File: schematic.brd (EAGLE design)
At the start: 50.5 x 50.8 mm, 32 parts, among them IC1 FT230XS, IC2 ATMEGA644A, IC4 L4931D, X1 MINI-USB-32005-301

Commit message: saving to git
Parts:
- added C11: .1uf, eagle-ltspice:C0504
- added C12, C13, C17: 1uF, eagle-ltspice:C0504
- added C14, C15: 2.2uF, eagle-ltspice:C0504
- added C16: .1uF, eagle-ltspice:C0504
- added R12, R13: 2K, eagle-ltspice:R0603
- added R14: 390K, eagle-ltspice:R0603
- added U$3: UG-2864HSWEG01, adafruit:1X30-0.7MM
- moved C10 29.2 mm to (64.8, 16.5)
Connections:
- new net N$10: C13.1, U$3.3
- new net N$11: C17.2, U$3.4
- new net N$12: C17.1, U$3.5
- new net N$5: C14.2, U$3.27
- new net N$7: C13.2, U$3.2
- new net N$9: R14.1, U$3.26
- new net OLED_SCL: R12.1, U$3.18
- new net OLED_SDA: R13.1, U$3.19, U$3.20
- new net OLED_VCC: C15.2, C16.2, U$3.28
- new net OLED_VDD: C11.2, C12.2, R12.2, R13.2, U$3.11, U$3.14, U$3.6, U$3.9
- new net OLED_VSS: U$3.10, U$3.12, U$3.13, U$3.16
- net GND: now also C11.1, C12.1, C14.1, C15.1, C16.1, R14.2, U$3.15, U$3.17, U$3.29, U$3.8

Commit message: saving
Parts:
- removed IC2: ATMEGA644A, atmel:TQFP44
- added C18: 1uF, eagle-ltspice:C0504
- added IC3: ATMEGA32U2-TQFP, adafruit:TQFP32-08
- added JP1: (no value), adafruit:1X06-BIG
- added R15, R16: 22, eagle-ltspice:R0603
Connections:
- removed net AVCC: IC2.27
- new net N$13: IC3.17, JP1.4
- new net N$14: C18.2, IC3.27
- new net N$15: IC3.30, R15.1
- new net N$16: IC3.29, R16.1
- new net N$3: IC3.15, JP1.2
- new net N$4: IC3.16, JP1.3
- new net RESET: IC3.24, JP1.5
- new net UGND: IC3.28, X1.4
- new net VUSB: C1.1, U$1.1, U$1.4, X1.1
- net B0: no longer IC2.11
- net B1: no longer IC2.12
- net B2: no longer IC2.13
- net GND: now also C18.1, IC3.3, JP1.6, U$3.1, U$3.30; no longer IC2.18, IC2.28, IC2.39, IC2.6, X1.4
- net OLED_VDD: no longer C11.2, C12.2, U$3.6, U$3.9
- net USB+: now also R16.2
- net USB-: now also R15.2
- net VCC: now also C11.2, C12.2, IC3.4, JP1.1, U$3.6, U$3.9; no longer IC2.17, IC2.38, IC2.5
- net VCHG: no longer C1.1, U$1.1, U$1.4, X1.1

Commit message: Saving to git
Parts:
- removed IC3: ATMEGA32U2-TQFP, adafruit:TQFP32-08
- removed R15, R16: 22, eagle-ltspice:R0603
- removed S1, S4, S5: (no value), switch-omron:B3F-10XX
- removed SV1: (no value), con-lsta:FE05-1
- removed U$2: RN4020, microchip_bluetooth_v101:RN4020SMD
- added JP2: (no value), pinhead:1X02
- added JP3: (no value), adafruit:1X03
- added LED1, LED2, LED3: (no value), adafruit:1206
- added R17, R18, R19: 2K, eagle-ltspice:R0603
- added SW1, SW2, SW3: (no value), adafruit:PUSHBUTTON_SMD_SJ
- added U$4: ATMEGA32U4-AU, adafruit:TQFP44
- U$1: value MCP73812T-420I/OT -> (none)
- moved C18 174.1 mm to (50.8, 67.3)
- moved JP1 174.1 mm to (64.1, 79.4)
- moved C14 101.1 mm to (54.0, 47.6)
- moved C15 101.1 mm to (54.0, 41.3)
- moved C16 101.1 mm to (54.0, 34.9)
- moved C17 101.1 mm to (54.0, 23.5)
- moved R14 101.1 mm to (54.0, 29.2)
- moved C12 81.8 mm to (59.7, 30.5)
- moved R13 81.8 mm to (59.7, 42.5)
- moved C11 81.8 mm to (59.7, 36.8)
- moved C13 81.8 mm to (59.7, 24.1)
- moved R12 81.8 mm to (59.7, 47.6)
- moved C6 15.3 mm to (40.0, 15.2)
- moved U$1 7.65 mm to (41.3, 38.1)
- moved C2 5.24 mm to (40.6, 12.7)
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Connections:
- removed net 6: IC1.4, R9.2
- removed net N$15: IC3.30, R15.1
- removed net N$16: IC3.29, R16.1
- removed net VCHG: C7.1, L1.2, SV1.5
- new net N$17: LED1.A, R17.1
- new net N$18: LED2.A, R18.1
- new net N$19: LED3.A, R19.1
- new net N$21: R19.2, U$4.29
- new net N$22: R18.2, U$4.30
- new net N$23: R17.2, U$4.12
- new net RXD: IC1.4, JP2.2, R9.2, U$4.20
- net B0: now also SW1.P$2, U$4.25; no longer S1.2
- net B1: now also SW2.P$2, U$4.22; no longer S4.2
- net B2: now also SW3.P$2, U$4.26; no longer S5.2
- net GND: now also JP3.3, LED1.C, LED2.C, LED3.C, U$4.15, U$4.23, U$4.35, U$4.43; no longer IC3.3, SV1.3
- net N$13: now also U$4.9; no longer IC3.17
- net N$14: now also U$4.6; no longer IC3.27
- net N$3: now also U$4.11; no longer IC3.15
- net N$4: now also U$4.10; no longer IC3.16
- net OLED_SCL: now also U$4.18
- net OLED_SDA: now also U$4.19
- net RESET: now also U$4.13; no longer IC3.24
- net TXD: now also JP2.1, U$4.21
- net UGND: now also U$4.5; no longer IC3.28
- net USB+: no longer R16.2
- net USB-: no longer R15.2
- net VBAT+: now also JP3.2; no longer SV1.4
- net VCC: now also C7.1, L1.2, SW1.P$1, SW2.P$1, SW3.P$1, U$4.14, U$4.24, U$4.34, U$4.44; no longer IC3.4, S1.3, S4.3, S5.3
- net VUSB: now also JP3.1, U$4.2, U$4.7

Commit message: Finished layout V1
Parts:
- removed JP2: (no value), pinhead:1X02
- removed R5: (no value), eagle-ltspice:R0603
- added JP4, JP5: (no value), adafruit:1X01
- L1: value BLM15HB221SN1 -> (none)
- R17, R18, R19: value 2K -> 330
- moved SW3 117.8 mm to (45.9, 24.3)
- moved SW1 97.2 mm to (46.0, 14.6)
- moved SW2 94.4 mm to (46.0, 5.11)
- moved LED3 82.0 mm to (35.0, 7.49)
- moved JP1 81.6 mm to (1.27, 27.3), turned to 90 degrees
- moved LED2 74.6 mm to (35.0, 5.59)
- moved LED1 67.4 mm to (35.0, 3.68)
- moved R19 65.9 mm to (31.2, 9.50), turned to 180 degrees
- moved R18 58.1 mm to (31.2, 5.51), turned to 180 degrees
- moved C12 54.3 mm to (5.97, 22.3), flipped to the bottom, turned to 270 degrees
- moved R17 52.3 mm to (31.1, 3.45), turned to 180 degrees
- moved R12 47.1 mm to (26.6, 14.1), turned to 180 degrees
- moved C13 46.0 mm to (14.7, 14.5), flipped to the bottom
- moved C18 44.6 mm to (25.0, 31.0), turned to 270 degrees
- moved JP3 44.3 mm to (1.27, 15.9), turned to 90 degrees
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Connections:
- net 2 renamed 9
- net 3 renamed 8
- removed net N$13: JP1.4, U$4.9
- removed net N$3: JP1.2, U$4.11
- removed net N$4: JP1.3, U$4.10
- removed net OLED_VCC: C15.2, C16.2, U$3.28
- removed net OLED_VSS: U$3.10, U$3.12, U$3.13, U$3.16
- removed net UGND: U$4.5, X1.4
- new net FTDI_VCC: IC1.12, L1.1
- new net MISO: JP1.3, U$4.11
- new net MOSI: JP1.4, U$4.10
- new net SCK: JP1.5, U$4.9
- net GND: now also U$3.10, U$3.12, U$3.13, U$3.16, U$4.5, X1.4
- net OLED_VDD: no longer U$3.11, U$3.14
- net RESET: now also JP1.2; no longer JP1.5
- net RXD: now also JP5.1; no longer JP2.2
- net TXD: now also JP4.1; no longer JP2.1
- net VCC: now also C15.2, C16.2, U$3.11, U$3.14, U$3.28; no longer IC1.12, L1.1
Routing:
- net GND: track 0.00 -> 230.1 mm, vias 0 -> 8
- net VCC: track 0.00 -> 132.5 mm, vias 0 -> 11
- net RXD: track 0.00 -> 53.1 mm, vias 0 -> 4
- net VUSB: track 0.00 -> 51.7 mm, vias 0 -> 4
- net TXD: track 0.00 -> 44.3 mm, vias 0 -> 3
- net N$22: track 0.00 -> 37.4 mm, vias 0 -> 4
- net NET1: track 0.00 -> 34.1 mm, vias 0 -> 4
- net N$23: track 0.00 -> 31.8 mm, vias 0 -> 3
- net RESET: track 0.00 -> 31.6 mm, vias 0 -> 2
- net N$21: track 0.00 -> 29.5 mm
- net SCK: track 0.00 -> 27.6 mm
- net MOSI: track 0.00 -> 26.8 mm
- net MISO: track 0.00 -> 26.1 mm
- net 8: track 0.00 -> 22.8 mm, vias 0 -> 2
- net B1: track 0.00 -> 22.1 mm, vias 0 -> 2
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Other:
- board size 50.5 x 50.8 mm -> 50.5 x 42 mm

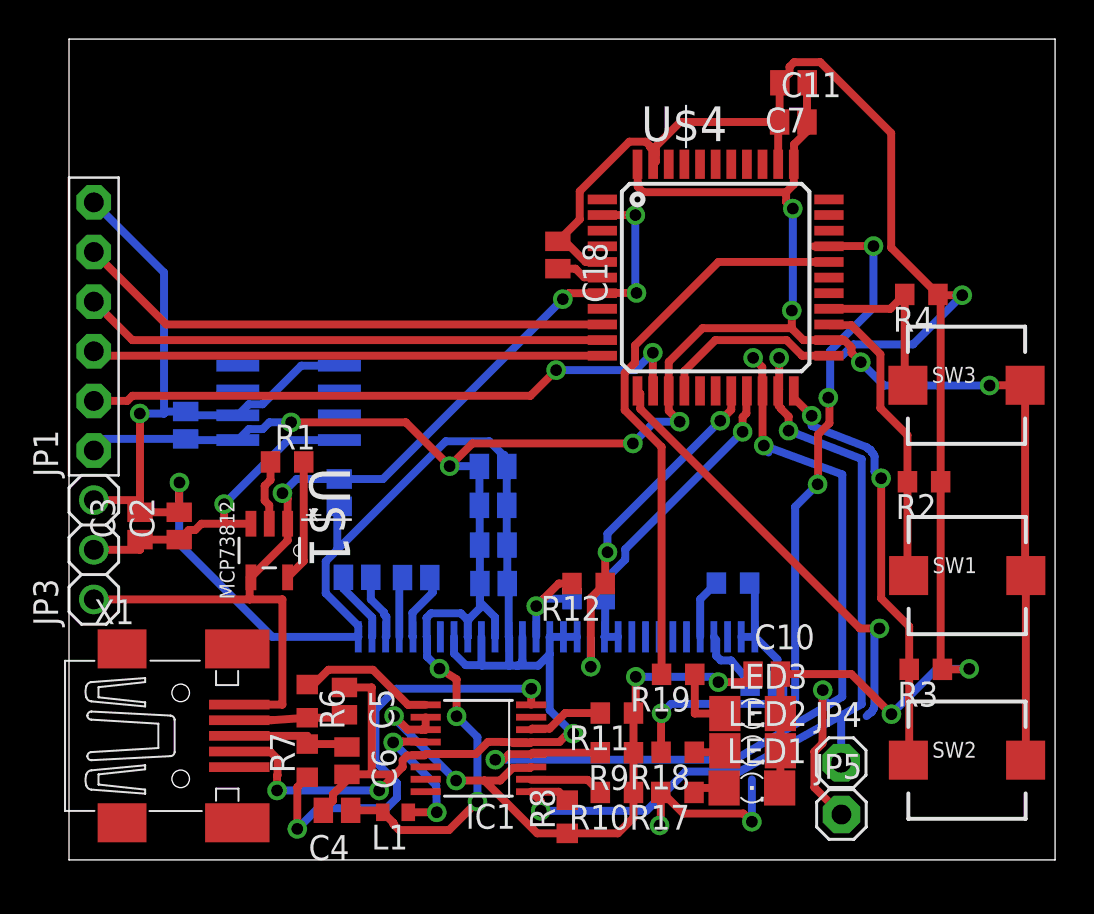
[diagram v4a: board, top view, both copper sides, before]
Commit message: Checked and fixed with OSH Park DRC
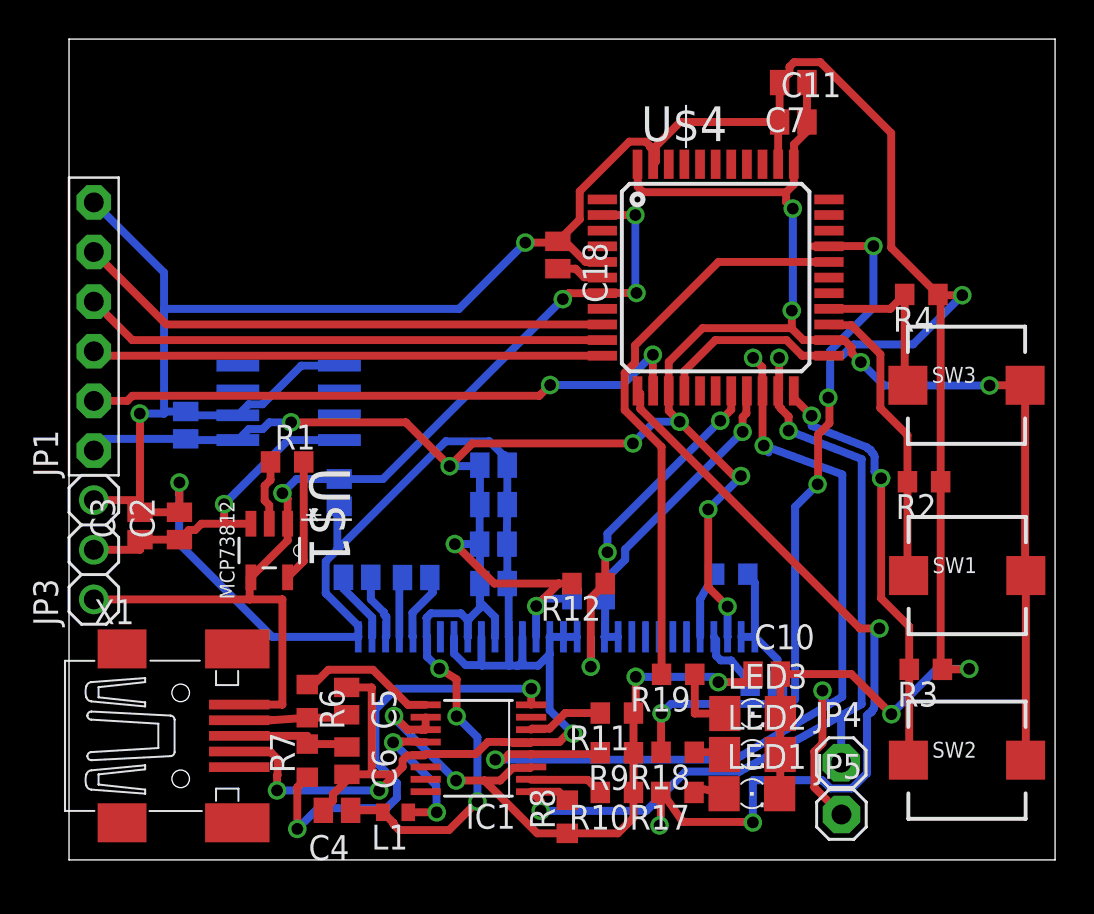
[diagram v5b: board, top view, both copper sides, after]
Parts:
- moved R14 0.47 mm to (33.9, 14.6)
- moved LED1 0.29 mm to (35.0, 3.39)
- moved LED2 0.19 mm to (35.0, 5.40)
- moved C5 0.11 mm to (14.2, 8.13)
- moved C9 0.07 mm to (21.7, 20.2)
- moved C15 0.05 mm to (21.7, 16.2)
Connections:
- removed net OLED_VDD: R12.2, R13.2
- net VCC: now also R12.2, R13.2
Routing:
- net VCC: track 132.5 -> 159.5 mm, vias 11 -> 16
- net GND: track 230.1 -> 252.3 mm, vias 8 -> 9
- net N$23: track 31.8 -> 41.7 mm
- net OLED_VDD: track 5.86 -> 0.00 mm, vias 1 -> 0

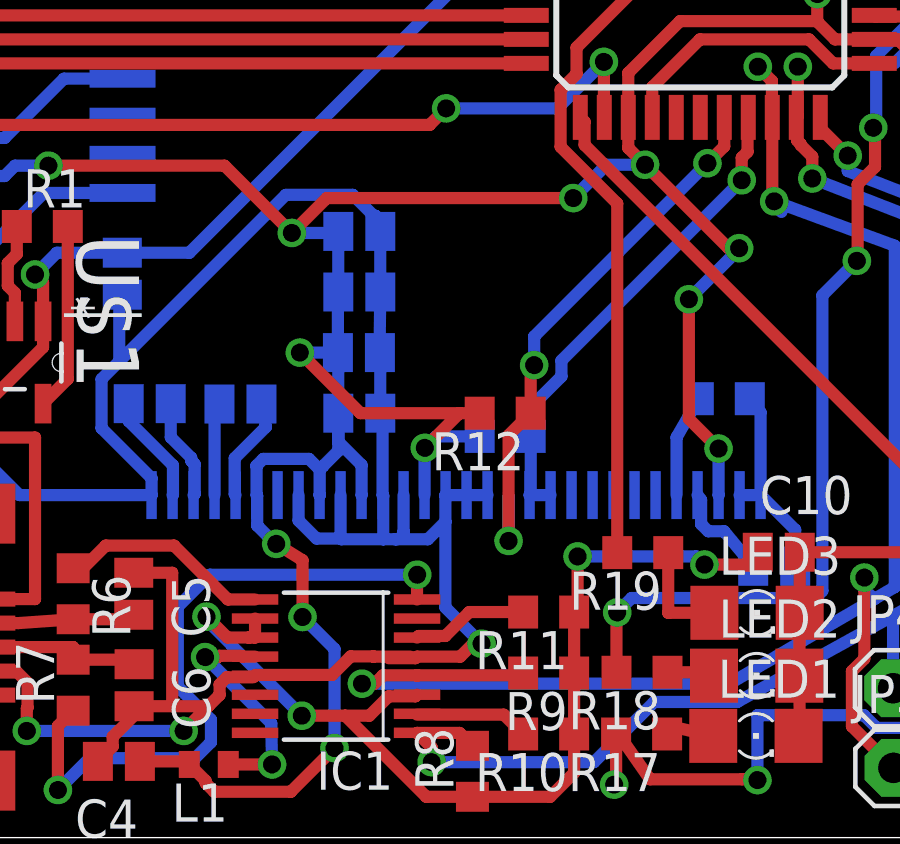
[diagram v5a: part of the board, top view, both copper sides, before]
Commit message: Added Power LED, passed DRC
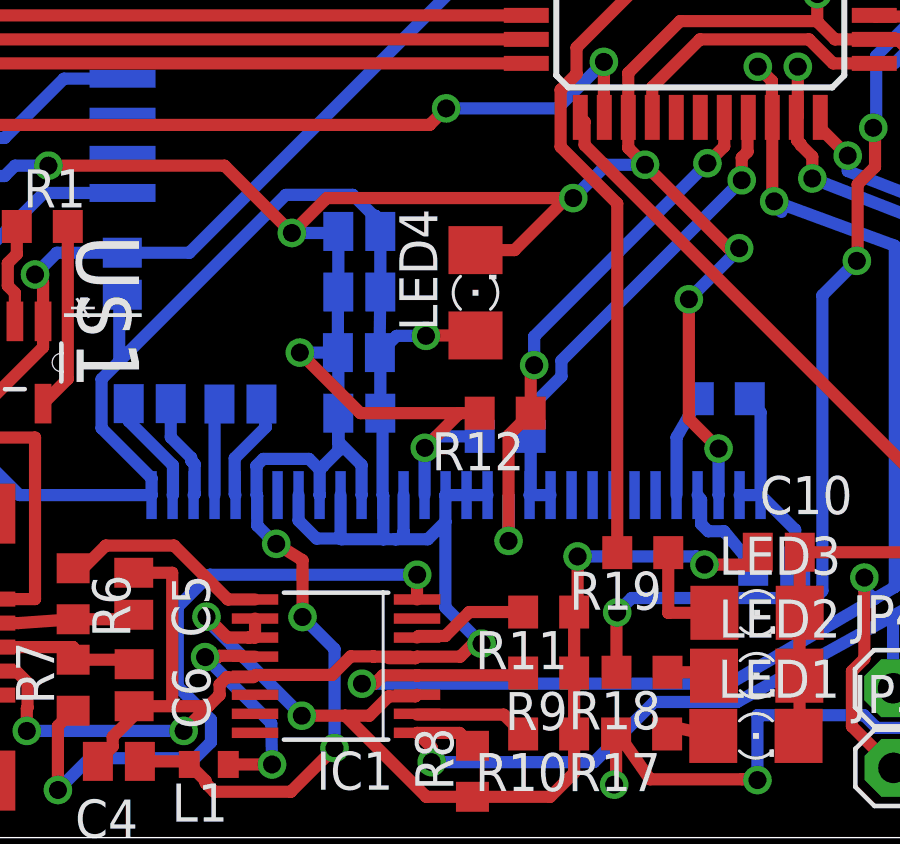
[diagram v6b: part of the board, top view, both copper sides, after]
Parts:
- added LED4: (no value), adafruit:1206
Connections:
- net GND: now also LED4.A
- net VCC: now also LED4.C
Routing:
- net VCC: track 159.5 -> 163.3 mm
- net GND: track 252.3 -> 255.7 mm, vias 9 -> 10
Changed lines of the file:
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@@
 <element name="JP4" library="adafruit" package="1X01" value="" x="39.5224" y="4.9784"/>
 <element name="JP5" library="adafruit" package="1X01" value="" x="39.5351" y="2.3241"/>
+<element name="LED4" library="adafruit" package="1206" value="" x="25.6032" y="18.161" rot="R90"/>
 </elements>
 <signals>
@@
 <wire x1="3.6322" y1="17.7942" x2="3.6322" y2="18.415" width="0.4064" layer="1"/>
 <wire x1="22.7116625" y1="5.9789" x2="23.6014" y2="5.9789" width="0.4064" layer="1"/>
-<wire x1="23.6014" y1="5.9789" x2="23.655" y2="6.0325" width="0.4064" layer="1"/>
+<wire x1="23.655" y1="6.0325" x2="23.6014" y2="5.9789" width="0.4064" layer="1"/>
 <wire x1="3.6322" y1="17.7942" x2="5.6515" y2="17.7942" width="0.4064" layer="1"/>
 <wire x1="36.4105" y1="7.493" x2="36.3978" y2="5.3975" width="0.4064" layer="1"/>
@@
 <wire x1="23.3553" y1="31.5976" x2="24.954" y2="31.5976" width="0.4064" layer="1"/>
 <wire x1="24.954" y1="31.5976" x2="25.019" y2="31.6626" width="0.4064" layer="1"/>
+<contactref element="LED4" pad="A"/>
+<wire x1="25.6032" y1="16.739" x2="23.9653" y2="16.739" width="0.4064" layer="1"/>
+<wire x1="23.9653" y1="16.739" x2="23.9522" y2="16.7259" width="0.4064" layer="1"/>
+<via x="23.9522" y="16.7259" extent="1-16" drill="0.6"/>
+<wire x1="23.9522" y1="16.7259" x2="22.9758" y2="16.7259" width="0.4064" layer="16"/>
+<wire x1="22.9758" y1="16.7259" x2="22.417" y2="16.1671" width="0.4064" layer="16"/>
 <wire x1="39.56953125" y1="25.8064" x2="38.8962" y2="25.8069" width="0" layer="19" extent="1-16"/>
 <wire x1="23.42789375" y1="6.0325" x2="23.6014" y2="5.9789" width="0" layer="19" extent="1-1"/>
@@
 <via x="19.4818" y="20.1549" extent="1-16" drill="0.6"/>
 <wire x1="19.4818" y1="20.1549" x2="20.64494375" y2="21.31804375" width="0.4064" layer="1"/>
-<wire x1="20.64494375" y1="21.31804375" x2="28.86184375" y2="21.31804375" width="0.4064" layer="1"/>
+<wire x1="28.6385" y1="21.31804375" x2="20.64494375" y2="21.31804375" width="0.4064" layer="1"/>
 <via x="28.86184375" y="21.31804375" extent="1-16" drill="0.6"/>
+<wire x1="28.6385" y1="21.31804375" x2="28.86184375" y2="21.31804375" width="0.4064" layer="1"/>
 <wire x1="28.86184375" y1="21.31804375" x2="29.972" y2="22.4282" width="0.4064" layer="16"/>
 <wire x1="29.972" y1="22.4282" x2="31.2547" y2="22.4282" width="0.4064" layer="16"/>
@@
 <wire x1="34.3916" y1="19.6469" x2="34.036" y2="19.6469" width="0.4064" layer="1"/>
 <wire x1="34.036" y1="19.6469" x2="31.2547" y2="22.4282" width="0.4064" layer="1"/>
+<contactref element="LED4" pad="C"/>
+<wire x1="25.6032" y1="19.583" x2="26.90345625" y2="19.583" width="0.4064" layer="1"/>
+<wire x1="26.90345625" y1="19.583" x2="28.6385" y2="21.31804375" width="0.4064" layer="1"/>
 </signal>
 <signal name="VBAT+">
